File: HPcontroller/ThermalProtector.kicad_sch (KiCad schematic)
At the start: 7 parts, among them U3 MIC841N

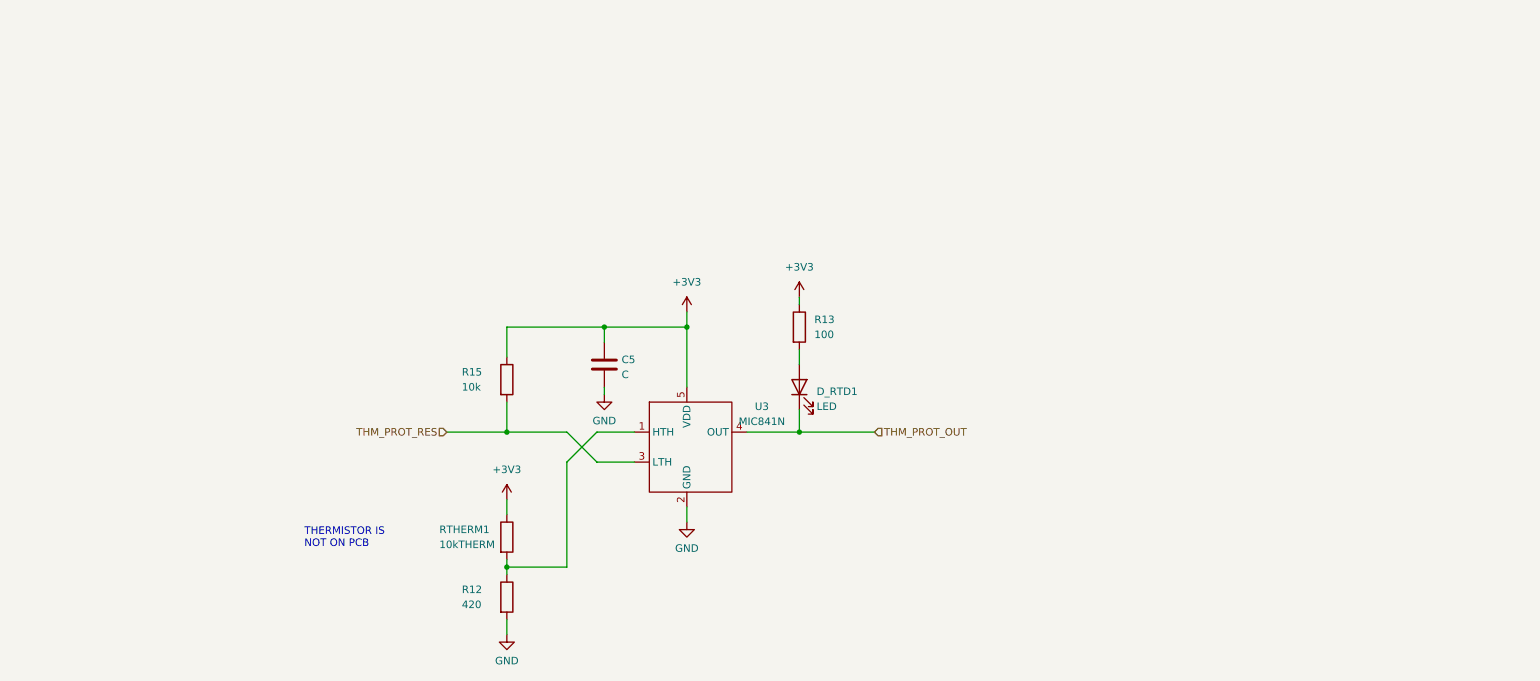
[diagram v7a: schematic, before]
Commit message: design "finished" need to do bom and footprints and layout
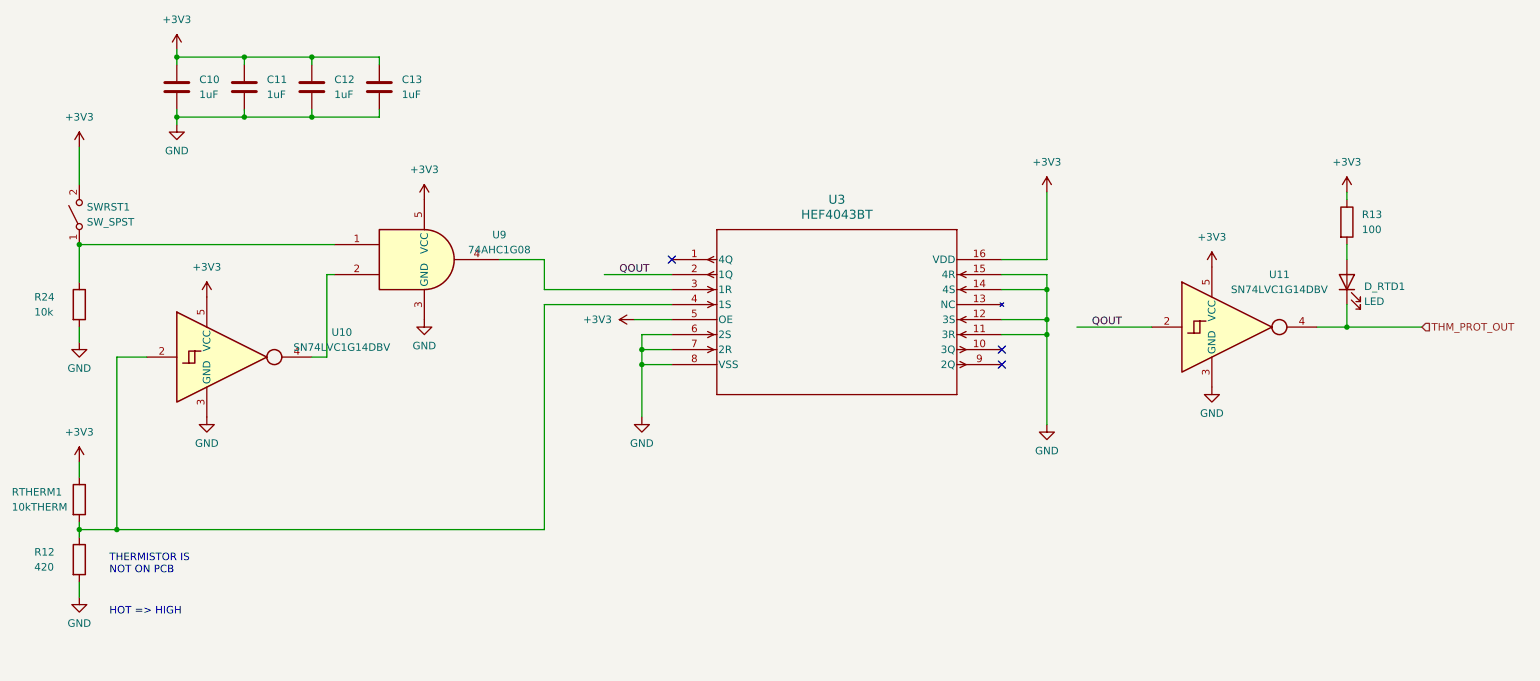
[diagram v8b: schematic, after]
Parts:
- removed C5: C, Capacitor_SMD:C_0805_2012Metric_Pad1.18x1.45mm_HandSolder, symbol Device:C
- removed R15: 10k, Resistor_SMD:R_0805_2012Metric_Pad1.20x1.40mm_HandSolder, symbol Device:R
- removed U3: MIC841N, Package_TO_SOT_SMD:SOT-353_SC-70-5_Handsoldering, symbol HPsym:MIC841N
- added C10, C11, C12, C13: 1uF, Capacitor_SMD:C_0805_2012Metric_Pad1.18x1.45mm_HandSolder, symbol Device:C
- added R24: 10k, Resistor_SMD:R_0805_2012Metric_Pad1.20x1.40mm_HandSolder, symbol Device:R
- added SWRST1: SW_SPST, Button_Switch_SMD:SW_SPST_PTS645, symbol Switch:SW_SPST
- added U10, U11: SN74LVC1G14DBV, Package_TO_SOT_SMD:SOT-23-5, symbol 74xGxx:SN74LVC1G14DBV
- added U3: HEF4043BT, SOT109-1_NXP, symbol HPsym:HEF4043BT
- added U9: 74AHC1G08, symbol 74xGxx:74AHC1G08
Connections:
- net +3V3: now also C10.1, C11.1, C12.1, C13.1, SWRST1.2 (B), U10.5 (VCC), U11.5 (VCC), U3.16 (VDD), U3.5 (OE), U9.5 (VCC)
- net GND: now also C10.2, C11.2, C12.2, C13.2, R24.2, U10.3 (GND), U11.3 (GND), U3.11 (3R), U3.12 (3S), U3.14 (4S), U3.15 (4R), U3.6 (2S), U3.7 (2R), U3.8 (VSS), U9.3 (GND)
- net THM_PROT_OUT: now also U11.4
- net at R12.1, RTHERM1.2: now also U10.2, U3.4 (1S)
- new net: R24.1, SWRST1.1 (A), U9.1
- new net: U3.3 (1R), U9.4
- new net: U10.4, U9.2
- new net QOUT: U11.2, U3.2 (1Q)
- no-connect marks 0 -> 3
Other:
- note added: "HOT => HIGH"
- moved on the sheet: D_RTD1, R12, R13, RTHERM1
